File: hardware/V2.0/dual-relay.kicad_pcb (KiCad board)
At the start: 2 copper layers, 45 x 45 mm, 26 parts, among them J101 AKL_5_2, J102 AKL_5_2, J103 AKL_5_2, P101 CON-SENSOR2, P102 BOOT, Q101 2N7002P, Q102 2N7002P, U101 XMC1XXX24, U102 DRILL, U103 DRILL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

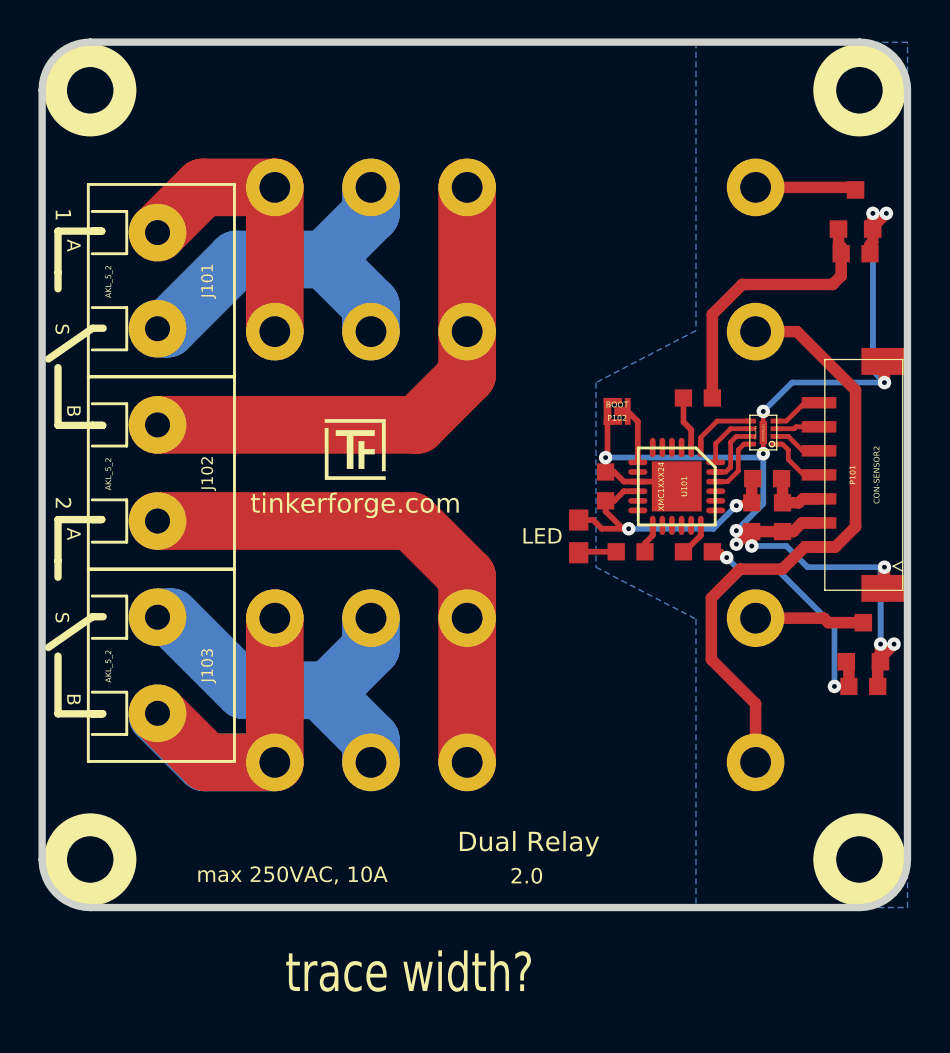
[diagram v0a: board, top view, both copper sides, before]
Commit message: change filtering to r/c circuit
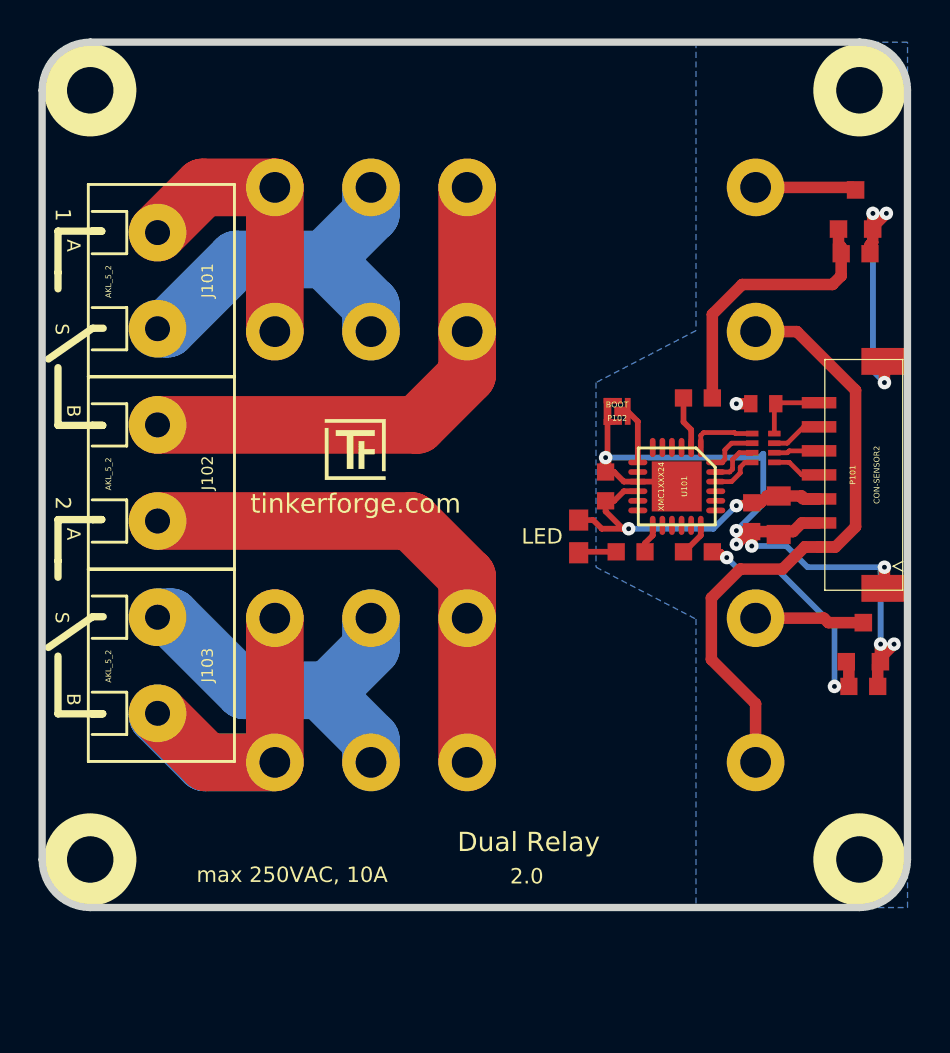
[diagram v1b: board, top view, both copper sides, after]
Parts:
- removed FB101: FILTER, R0603F
- removed FILTER101: Filter-4x, kicad-libraries:DFN8-17x135
- added C104: 100nF, C0603F, F.Cu at (156.4, 104.8)
- added RP101: TBD, kicad-libraries:4X0402, F.Cu at (164.6, 102.8)
- C102: footprint C0603F -> C0402E
- C103: value 100nF -> 10uF; footprint C0603F -> C0805
- moved C103 9.12 mm to (165.4, 106.3)
- moved C102 5.93 mm to (164.6, 100.5), turned to 0 degrees
- moved C101 1.60 mm to (164.0, 106.4)
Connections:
- C101 pad 2: Net-(C101-Pad2) -> VCC
- C102 pad 2: VCC -> Net-(C102-Pad2)
- C103 pad 1: VCC -> GND
- C103 pad 2: GND -> VCC
- P101 pad 3: Net-(C101-Pad2) -> VCC
- P101 pad 7: Net-(FILTER101-Pad4) -> Net-(C102-Pad2)
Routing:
- net GND: track 69.9 -> 61.5 mm, vias 12 -> 11
- net Net-(C102-Pad2): track 0.00 -> 4.60 mm
- net VCC: track 15.0 -> 18.3 mm
- net Net-(C101-Pad2): track 3.25 -> 0.00 mm
- net Net-(FILTER101-Pad4): track 2.62 -> 0.00 mm
- net S-CS: track 3.25 -> 2.49 mm
- net S-CLK: track 3.33 -> 2.61 mm
- net Net-(P101-Pad4): track 3.18 -> 2.59 mm
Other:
- board text removed: "trace width?"

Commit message: add fiducials, logos, protection diodes
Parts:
- added D102: LL4148, MiniMelf, F.Cu at (168.3, 95.1)
- added D103: LL4148, MiniMelf, F.Cu at (168.4, 117.5)
- added Fiducial_Mark: VAL**, kicad-libraries:Fiducial_Mark, F.Cu at (170.6, 119.7)
- added Fiducial_Mark: VAL**, kicad-libraries:Fiducial_Mark, F.Cu at (165.1, 83.2)
- added Fiducial_Mark: VAL**, kicad-libraries:Fiducial_Mark, F.Cu at (149.1, 104.2)
- added G***: LOGO, kicad-libraries:Logo_CoMCU, B.Cu at (152.1, 104.2)
- added G***: LOGO, kicad-libraries:WEEE_7mm, B.Cu at (160.6, 104.2)
- added VAL: CE_5mm, kicad-libraries:CE_5mm, B.Cu at (142.6, 104.2)
- P101: footprint CON-SENSOR2 -> kicad-libraries:CON-SENSOR2
- moved R105 1.20 mm to (170.7, 116.0), turned to 270 degrees
- moved R104 1.06 mm to (170.2, 92.0)
- moved Q101 0.80 mm to (169.4, 89.6)
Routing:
- net Net-(D102-Pad1): track 5.26 -> 12.9 mm
- net Net-(D103-Pad1): track 5.70 -> 12.2 mm
- net +5V: track 32.1 -> 37.4 mm
- net Net-(Q101-PadG): track 14.4 -> 17.2 mm
- net Net-(Q102-PadG): track 13.2 -> 15.4 mm
